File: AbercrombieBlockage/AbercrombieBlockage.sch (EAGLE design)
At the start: 13 parts, among them U1 CY8CKIT-142, U2 DMN3135LVT, U3 DMN3135LVT, U4 DMN3135LVT

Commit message: Added the Abercrombie board.
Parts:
- removed LED6: LG_T679-E1F1-1, led:LG_T679-E1F1-1
- added C3: 10u, resistor:C-USC1210
- added C4, C5: 1u, resistor:C-USC0603
- added C6: 5p, resistor:C-USC0603
- added D1: BPW34, NicksParts:BPW34
- added R2: 20k, resistor:R-US_R0603
- added R3, R5, R6: DNP, resistor:R-US_R0603
- added R4: 0, resistor:R-US_R0603
- added SV1, SV2: (no value), con-lstb:MA03-1
- added SV3: (no value), con-lstb:MA05-1
- added TP1, TP2, TP3: TPB1,27, testpad:TPB1,27
- added U5: M95M01, NicksParts:M95M01
- added U6: LDK130M-R, NicksParts:LDK130M-R
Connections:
- removed net LED6: U4.G2
- new net CS: U1.P1.5, U5.CS
- new net HOLD: U1.P0.4, U5.HOLD
- new net MISO: U1.P1.6, U5.MISO
- new net MOSI: U1.P1.7, U5.MOSI
- new net N$10: R5.2, R6.1, TP1.TP, U6.ADJ
- new net N$11: C6.1, D1.C, R2.2, U1.P2.1
- new net N$13: R3.2, R4.1, U1.P2.0
- new net N$9: C6.2, R2.1, U1.P2.2
- new net SCLK: U1.P1.3, U5.CLK
- new net SWDCLK: SV3.4, U1.P0.7
- new net SWDIO: SV3.5, U1.P0.6
- new net VBATT: C1.1, C2.1, C4.1, R1.2, SV1.3, SV2.3, U6.EN, U6.IN
- new net VREF: TP2.TP, U1.VREF
- new net WP: U1.P1.4, U5.WP
- new net XRES: SV3.3, TP3.TP, U1.XRES
- net GND: now also C3.2, C4.2, C5.2, D1.A, R4.2, R6.2, SV1.1, SV3.2, U1.GND1, U1.GND2, U6.GND
- net LED1: now also U1.P3.6
- net LED2: now also U1.P3.4
- net LED3: now also U1.P3.2
- net LED4: now also U1.P3.0
- net LED5: now also U1.P4.0
- net N$1: no longer LED6.A
- net N$7: now also C3.1, C5.1, R5.1, SV2.1, U6.OUT; no longer LED6.C, U4.D2
- net VCC: now also R3.1, SV2.2, SV3.1, U1.VDDA, U1.VDDD, U1.VDDR, U5.VCC; no longer C1.1, C2.1, R1.2
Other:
- moved on the sheet: C1, C2, U1

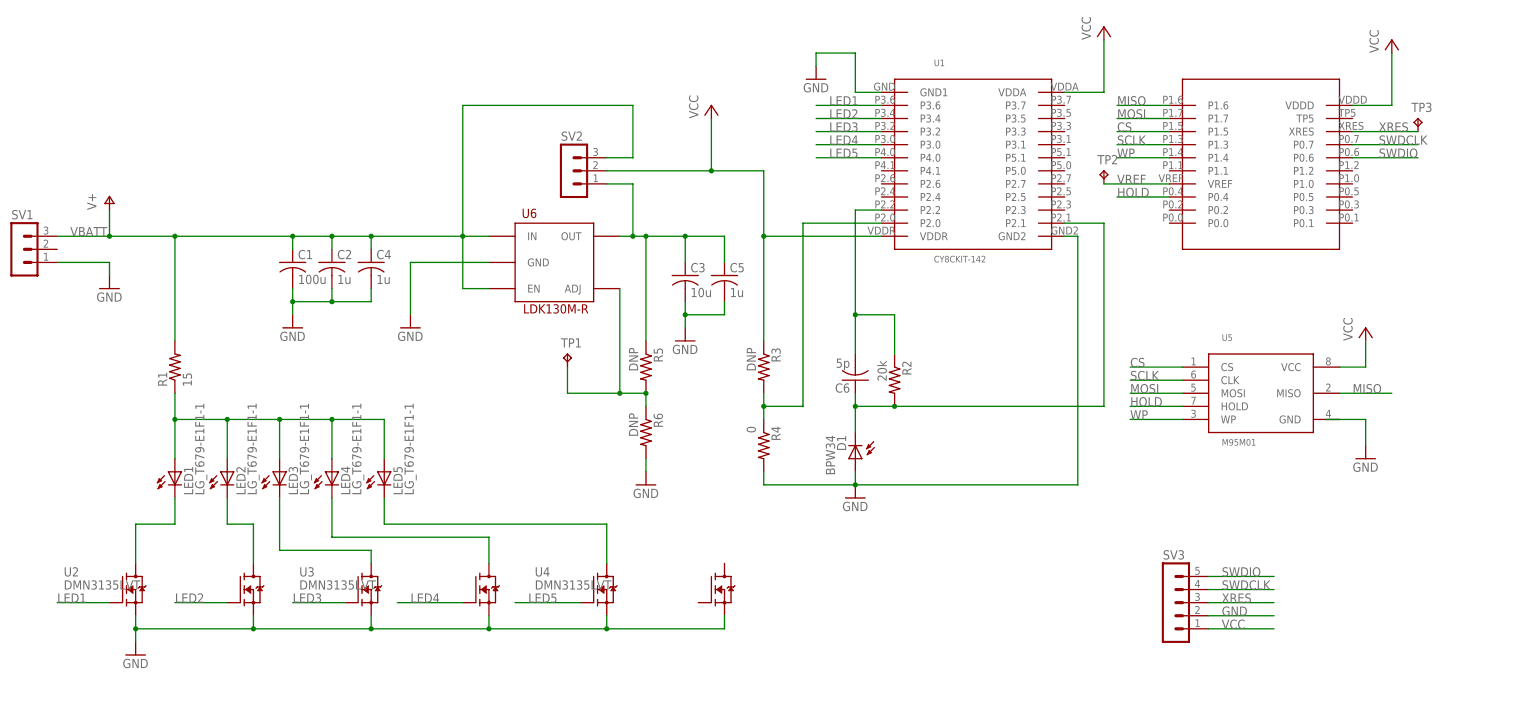
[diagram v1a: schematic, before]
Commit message: Finished the schematic and placement. Starting routing for Abercrombie.
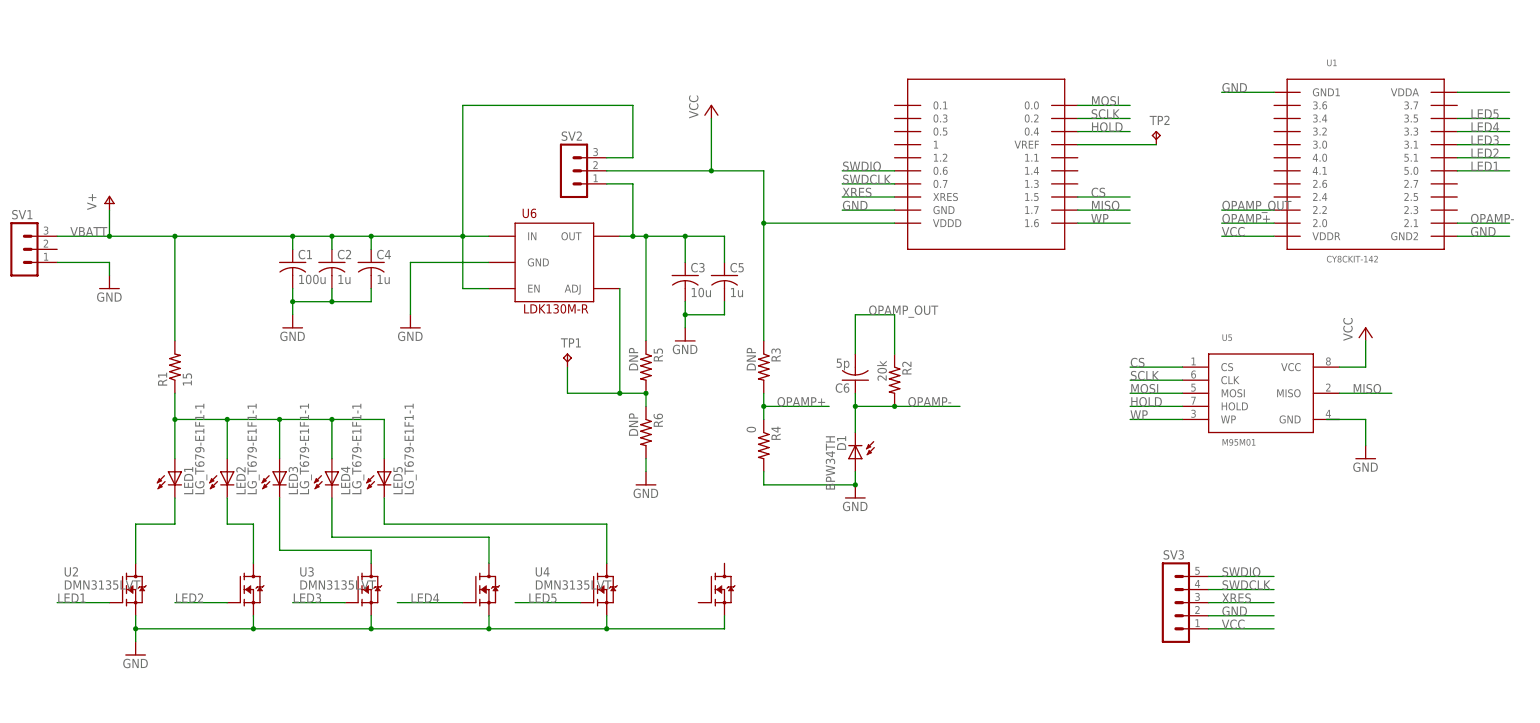
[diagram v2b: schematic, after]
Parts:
- removed TP3: TPB1,27, testpad:TPB1,27
- D1: value BPW34 -> BPW34TH; device NicksParts:BPW34 -> NicksParts:BPW34TH
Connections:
- removed net N$11: C6.1, D1.C, R2.2, U1.P2.1
- removed net N$13: R3.2, R4.1, U1.P2.0
- removed net N$9: C6.2, R2.1, U1.P2.2
- new net OPAMP+: R3.2, R4.1, U1.2.0
- new net OPAMP-: C6.1, D1.C, R2.2, U1.2.1
- new net OPAMP_OUT: C6.2, R2.1, U1.2.2
- net CS: now also U1.1.5; no longer U1.P1.5
- net GND: now also U1.GND
- net HOLD: now also U1.0.4; no longer U1.P0.4
- net LED1: now also U1.5.0; no longer U1.P3.6
- net LED2: now also U1.5.1; no longer U1.P3.4
- net LED3: now also U1.3.1; no longer U1.P3.2
- net LED4: now also U1.3.3; no longer U1.P3.0
- net LED5: now also U1.3.5; no longer U1.P4.0
- net MISO: now also U1.1.7; no longer U1.P1.6
- net MOSI: now also U1.0.0; no longer U1.P1.7
- net SCLK: now also U1.0.2; no longer U1.P1.3
- net SWDCLK: now also U1.0.7; no longer U1.P0.7
- net SWDIO: now also U1.0.6; no longer U1.P0.6
- net VREF: no longer U1.VREF
- net WP: now also U1.1.6; no longer U1.P1.4
- net XRES: no longer TP3.TP
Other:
- moved on the sheet: TP2

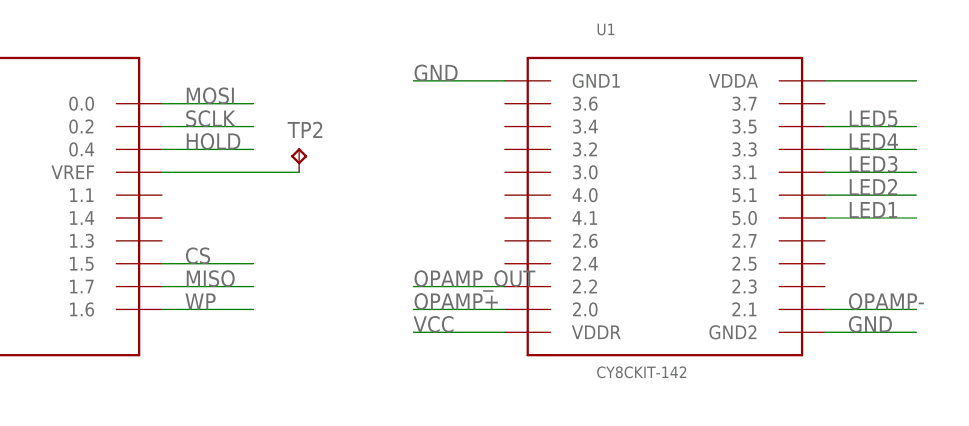
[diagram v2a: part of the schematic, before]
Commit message: Fully routed Abercrombie design
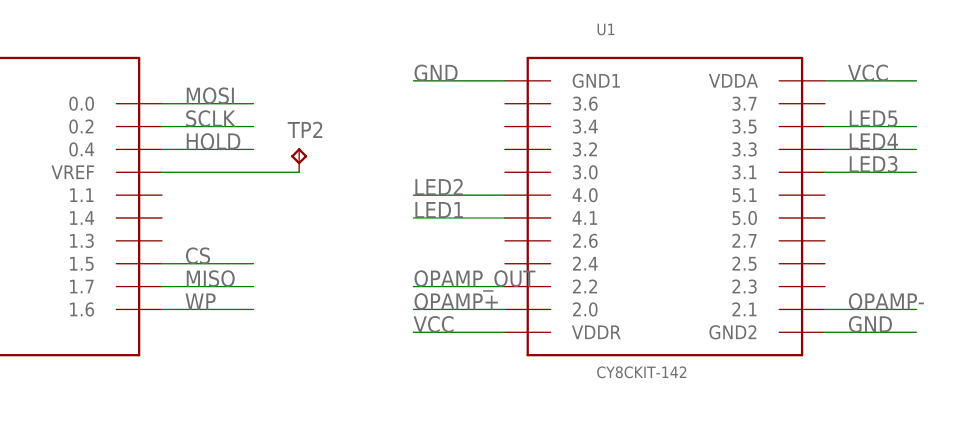
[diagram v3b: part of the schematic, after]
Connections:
- removed net VREF: TP2.TP
- new net N$9: TP2.TP, U1.VREF
- net LED1: now also U1.4.1; no longer U1.5.0
- net LED2: now also U1.4.0; no longer U1.5.1
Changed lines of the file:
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@@
 <part name="GND8" library="supply1" deviceset="GND" device=""/>
 <part name="TP1" library="testpad" deviceset="TP" device="B1,27"/>
-<part name="TP2" library="testpad" deviceset="TP" device="B1,27"/>
 <part name="R5" library="resistor" deviceset="R-US_" device="R0603" value="DNP"/>
 <part name="R6" library="resistor" deviceset="R-US_" device="R0603" value="DNP"/>
@@
 <part name="SV3" library="con-lstb" deviceset="MA05-1" device=""/>
 <part name="U1" library="NicksParts" deviceset="CY8CKIT-142" device=""/>
+<part name="TP2" library="testpad" deviceset="TP" device="B1,27"/>
 </parts>
 <sheets>
@@
 <instance part="GND8" gate="1" x="251.46" y="43.18"/>
 <instance part="TP1" gate="G$1" x="96.52" y="63.5"/>
-<instance part="TP2" gate="G$1" x="210.82" y="106.68"/>
 <instance part="R5" gate="G$1" x="111.76" y="60.96" rot="R270"/>
 <instance part="R6" gate="G$1" x="111.76" y="48.26" rot="R270"/>
@@
 <instance part="SV3" gate="G$1" x="213.36" y="15.24"/>
 <instance part="U1" gate="G$1" x="215.9" y="101.6"/>
+<instance part="TP2" gate="G$1" x="210.82" y="106.68"/>
 </instances>
 <busses>
@@
 </segment>
 <segment>
-<pinref part="U1" gate="G$1" pin="5.0"/>
-<wire x1="269.24" y1="99.06" x2="279.4" y2="99.06" width="0.1524" layer="91"/>
-<label x="271.78" y="99.06" size="1.778" layer="95"/>
+<pinref part="U1" gate="G$1" pin="4.1"/>
+<wire x1="233.68" y1="99.06" x2="223.52" y2="99.06" width="0.1524" layer="91"/>
+<label x="223.52" y="99.06" size="1.778" layer="95"/>
 </segment>
 </net>
@@
 </segment>
 <segment>
-<pinref part="U1" gate="G$1" pin="5.1"/>
-<wire x1="269.24" y1="101.6" x2="279.4" y2="101.6" width="0.1524" layer="91"/>
-<label x="271.78" y="101.6" size="1.778" layer="95"/>
+<pinref part="U1" gate="G$1" pin="4.0"/>
+<wire x1="233.68" y1="101.6" x2="223.52" y2="101.6" width="0.1524" layer="91"/>
+<label x="223.52" y="101.6" size="1.778" layer="95"/>
 </segment>
 </net>
@@
 <pinref part="U1" gate="G$1" pin="VDDA"/>
 <wire x1="269.24" y1="114.3" x2="279.4" y2="114.3" width="0.1524" layer="91"/>
+<label x="271.78" y="114.3" size="1.778" layer="95"/>
 </segment>
 </net>
@@
 <wire x1="195.58" y1="106.68" x2="205.74" y2="106.68" width="0.1524" layer="91"/>
 <label x="198.12" y="106.68" size="1.778" layer="95"/>
-</segment>
-</net>
-<net name="VREF" class="0">
-<segment>
-<wire x1="195.58" y1="104.14" x2="210.82" y2="104.14" width="0.1524" layer="91"/>
-<pinref part="TP2" gate="G$1" pin="TP"/>
 </segment>
 </net>
@@
 </segment>
 </net>
+<net name="N$9" class="0">
+<segment>
+<pinref part="TP2" gate="G$1" pin="TP"/>
+<pinref part="U1" gate="G$1" pin="VREF"/>
+<wire x1="210.82" y1="104.14" x2="195.58" y2="104.14" width="0.1524" layer="91"/>
+</segment>
+</net>
 </nets>
 </sheet>
 </sheets>
+<errors>
+</errors>
 </schematic>
 </drawing>

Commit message: Added digikey part numbers for the various components.
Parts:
- LED1: DIGIKEY2 (none) -> VSMY2850GCT-ND
- R1: DIGIKEY_100_OHM (none) -> YAG3381CT-ND; DIGIKEY_30_OHM (none) -> RHM30BGCT-ND; DIGIKEY_50_OHM (none) -> 541-2477-1-ND
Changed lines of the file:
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@@
 <part name="LED1" library="led" deviceset="*_T679-?-1" device="E1F1" technology="LG">
 <attribute name="DIGIKEY" value="VSMY3850-GS08CT-ND"/>
+<attribute name="DIGIKEY2" value="VSMY2850GCT-ND"/>
 </part>
 <part name="C1" library="resistor" deviceset="C-US" device="C1210" value="100u"/>
 <part name="C2" library="resistor" deviceset="C-US" device="C1210" value="1u"/>
-<part name="R1" library="resistor" deviceset="R-US_" device="R2010" value="15"/>
+<part name="R1" library="resistor" deviceset="R-US_" device="R2010" value="15">
+<attribute name="DIGIKEY_100_OHM" value="YAG3381CT-ND"/>
+<attribute name="DIGIKEY_30_OHM" value="RHM30BGCT-ND"/>
+<attribute name="DIGIKEY_50_OHM" value="541-2477-1-ND"/>
+</part>
 <part name="P+1" library="supply1" deviceset="VCC" device=""/>
 <part name="LED2" library="led" deviceset="*_T679-?-1" device="E1F1" technology="LG">
@@
 <instance part="LED1" gate="G$1" x="20.32" y="40.64">
 <attribute name="DIGIKEY" x="20.32" y="40.64" size="1.778" layer="96" display="off"/>
+<attribute name="DIGIKEY2" x="20.32" y="40.64" size="1.778" layer="96" display="off"/>
 </instance>
 <instance part="C1" gate="G$1" x="43.18" y="81.28"/>
 <instance part="C2" gate="G$1" x="50.8" y="81.28"/>
-<instance part="R1" gate="G$1" x="20.32" y="60.96" rot="R90"/>
+<instance part="R1" gate="G$1" x="20.32" y="60.96" rot="R90">
+<attribute name="DIGIKEY_100_OHM" x="20.32" y="60.96" size="1.778" layer="96" rot="R90" display="off"/>
+<attribute name="DIGIKEY_30_OHM" x="20.32" y="60.96" size="1.778" layer="96" rot="R90" display="off"/>
+<attribute name="DIGIKEY_50_OHM" x="20.32" y="60.96" size="1.778" layer="96" rot="R90" display="off"/>
+</instance>
 <instance part="P+1" gate="VCC" x="124.46" y="111.76"/>
 <instance part="LED2" gate="G$1" x="30.48" y="40.64">

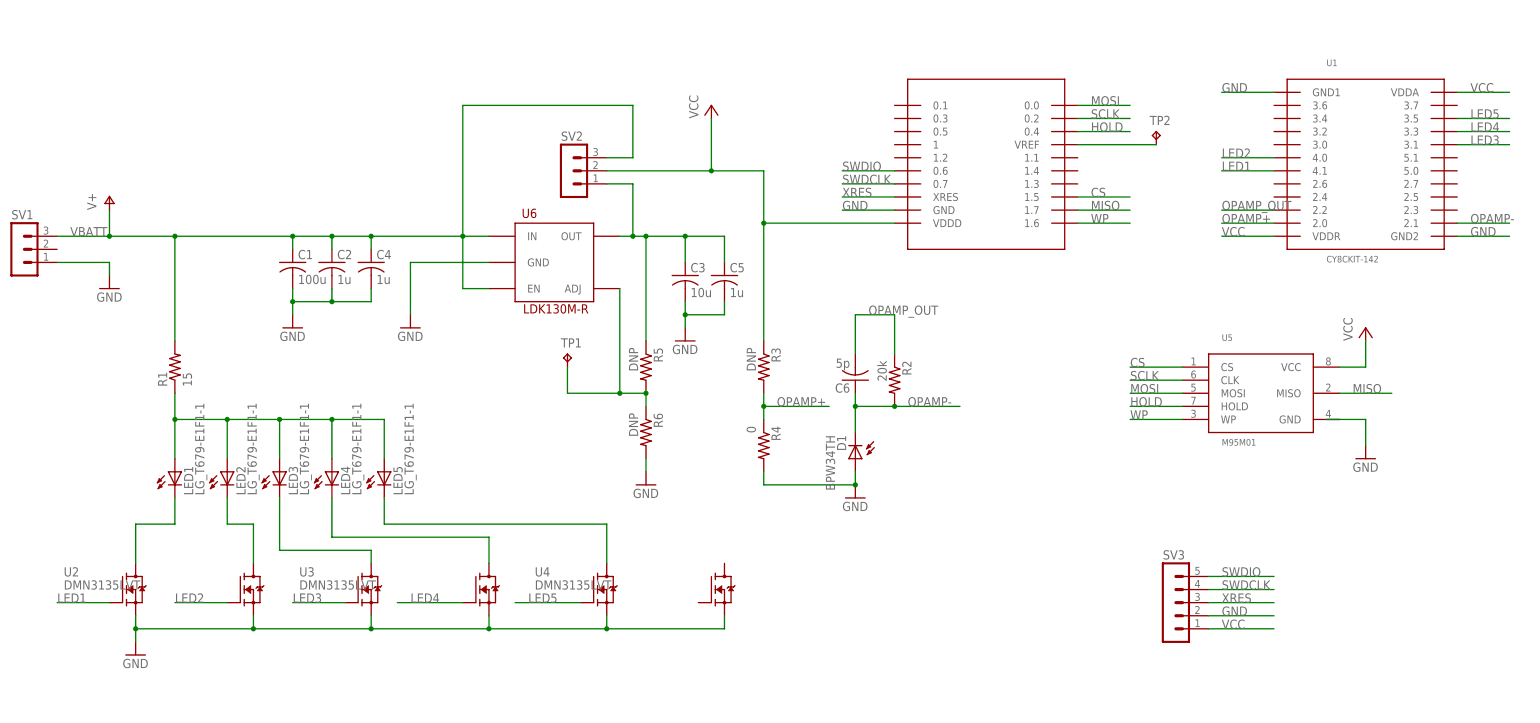
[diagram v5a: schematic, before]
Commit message: Updated to fix issues with the layout.
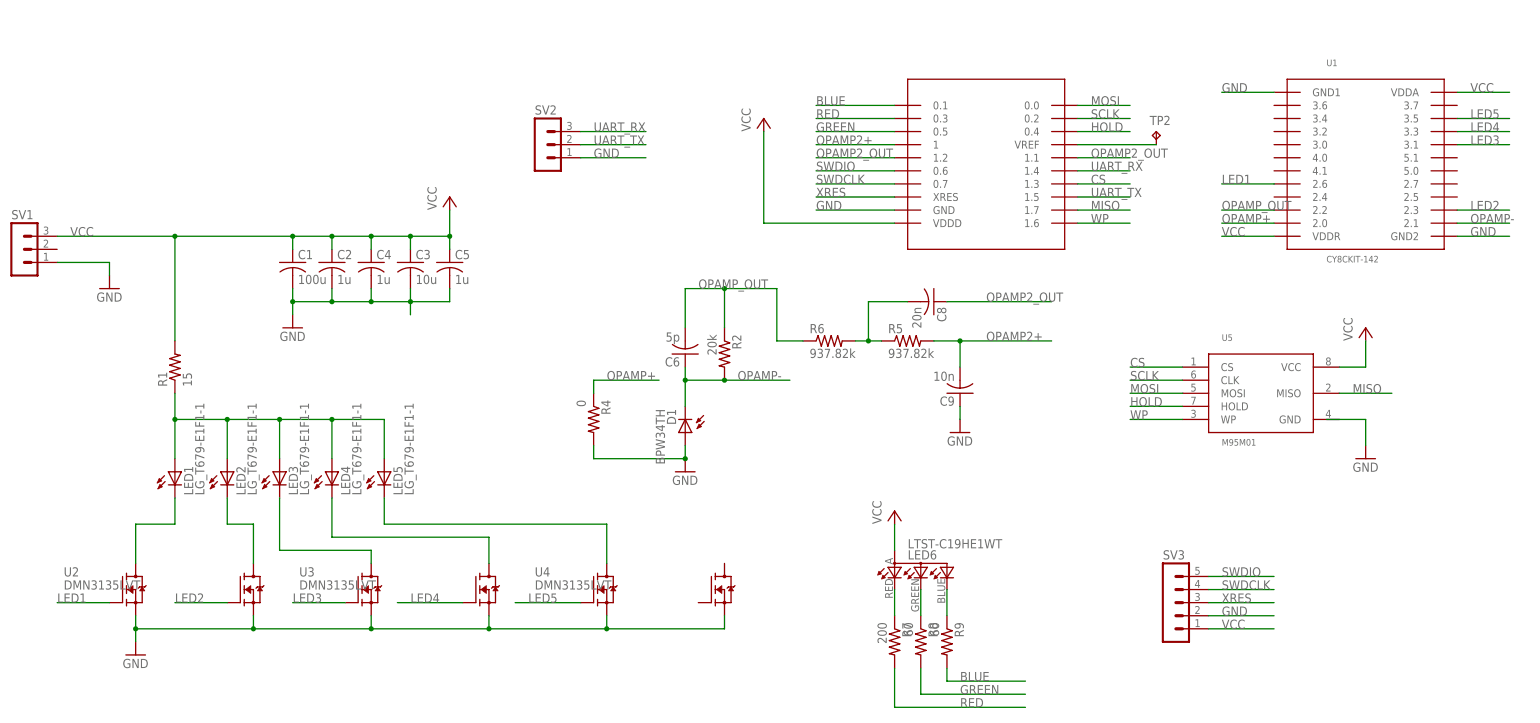
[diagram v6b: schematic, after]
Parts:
- removed R3: DNP, resistor:R-US_R0603
- removed TP1: TPB1,27, testpad:TPB1,27
- removed U6: LDK130M-R, NicksParts:LDK130M-R
- added C8: 20n, resistor:C-USC0603
- added C9: 10n, resistor:C-USC0603
- added LED6: LTST-C19HE1WT, NicksParts:LTST-C19HE1WT
- added R7: 200, resistor:R-US_R0603
- added R8, R9: 60, resistor:R-US_R0603
- R5, R6: value DNP -> 937.82k
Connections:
- removed net VBATT: C1.1, C2.1, C4.1, R1.2, SV1.3, SV2.3, U6.EN, U6.IN
- new net BLUE: R9.2, U1.0.1
- new net GREEN: R8.2, U1.0.5
- new net N$11: LED6.CGREEN, R8.1
- new net N$13: LED6.CBLUE, R9.1
- new net OPAMP2+: C9.2, R5.2, U1.1
- new net OPAMP2_OUT: C8.1, U1.1.1, U1.1.2
- new net RED: R7.2, U1.0.3
- new net UART_RX: SV2.3, U1.1.4
- new net UART_TX: SV2.2, U1.1.5
- net CS: now also U1.1.3; no longer U1.1.5
- net GND: now also C9.1, SV2.1; no longer R6.2, U6.GND
- net LED1: now also U1.2.6; no longer U1.4.1
- net LED2: now also U1.2.3; no longer U1.4.0
- net N$10: now also LED6.CRED, R7.1; no longer R5.2, R6.1, TP1.TP, U6.ADJ
- net N$7: now also C8.2, R6.2; no longer C3.1, C5.1, SV2.1, U6.OUT
- net OPAMP+: no longer R3.2
- net OPAMP_OUT: now also R6.1
- net VCC: now also C1.1, C2.1, C3.1, C4.1, C5.1, LED6.A, R1.2, SV1.3; no longer R3.1, SV2.2
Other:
- moved on the sheet: C3, C5, C6, D1, R2, R4, R5, R6, SV2

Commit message: Updated Abercrombie values.
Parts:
- C1: value 100u -> 220u
- C2: value 1u -> 220u
- C8: value 20n -> 0
- C9: value 10n -> 620K
- R5: value 937.82k -> 1M
- R6: value 937.82k -> DNP
- R7: value 200 -> 360
- R8, R9: value 60 -> 360
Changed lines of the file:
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@@
 <attribute name="DIGIKEY2" value="VSMY2850GCT-ND"/>
 </part>
-<part name="C1" library="resistor" deviceset="C-US" device="C1210" value="100u"/>
-<part name="C2" library="resistor" deviceset="C-US" device="C1210" value="1u"/>
+<part name="C1" library="resistor" deviceset="C-US" device="C1210" value="220u"/>
+<part name="C2" library="resistor" deviceset="C-US" device="C1210" value="220u"/>
 <part name="R1" library="resistor" deviceset="R-US_" device="R2010" value="15">
 <attribute name="DIGIKEY_100_OHM" value="YAG3381CT-ND"/>
@@
 <part name="LED6" library="NicksParts" deviceset="LTST-C19HE1WT" device=""/>
 <part name="GND4" library="supply1" deviceset="GND" device=""/>
-<part name="C8" library="resistor" deviceset="C-US" device="C0603" value="20n"/>
-<part name="R5" library="resistor" deviceset="R-US_" device="R0603" value="937.82k"/>
-<part name="R6" library="resistor" deviceset="R-US_" device="R0603" value="937.82k"/>
-<part name="C9" library="resistor" deviceset="C-US" device="C0603" value="10n"/>
-<part name="R7" library="resistor" deviceset="R-US_" device="R0603" value="200"/>
-<part name="R8" library="resistor" deviceset="R-US_" device="R0603" value="60"/>
-<part name="R9" library="resistor" deviceset="R-US_" device="R0603" value="60"/>
+<part name="C8" library="resistor" deviceset="C-US" device="C0603" value="0"/>
+<part name="R5" library="resistor" deviceset="R-US_" device="R0603" value="1M"/>
+<part name="R6" library="resistor" deviceset="R-US_" device="R0603" value="DNP"/>
+<part name="C9" library="resistor" deviceset="C-US" device="C0603" value="620K"/>
+<part name="R7" library="resistor" deviceset="R-US_" device="R0603" value="360"/>
+<part name="R8" library="resistor" deviceset="R-US_" device="R0603" value="360"/>
+<part name="R9" library="resistor" deviceset="R-US_" device="R0603" value="360"/>
 <part name="P+2" library="supply1" deviceset="VCC" device=""/>
 </parts>
